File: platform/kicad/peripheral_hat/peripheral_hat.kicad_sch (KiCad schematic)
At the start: 48 parts, among them J1 Pi Header, J2 Pogo Pin, J3 Pogo Pin, J4 CRJ032-1-TH, J5 JST EH, J6 JST EH, T1 PT61018PEL, U1 LAN9500A-ABZJ

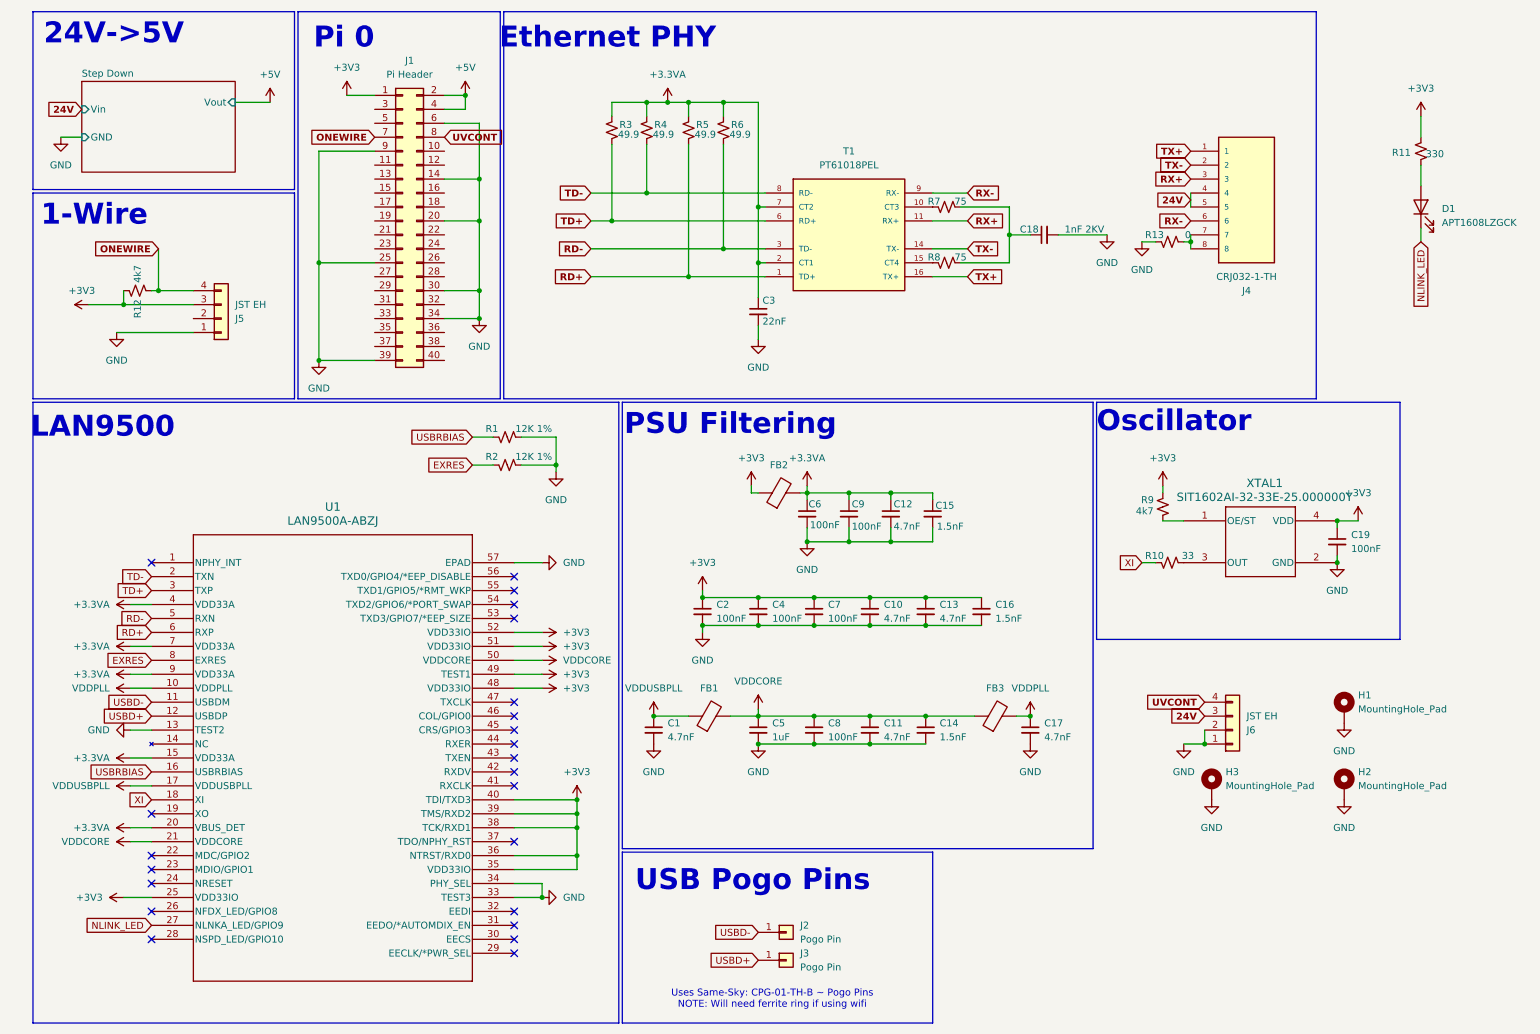
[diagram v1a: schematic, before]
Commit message: Peripheral Hat: Add MEMS I2C connector
This change adds a 5pin JST EH connector for connecting a I2S MEMS
device.
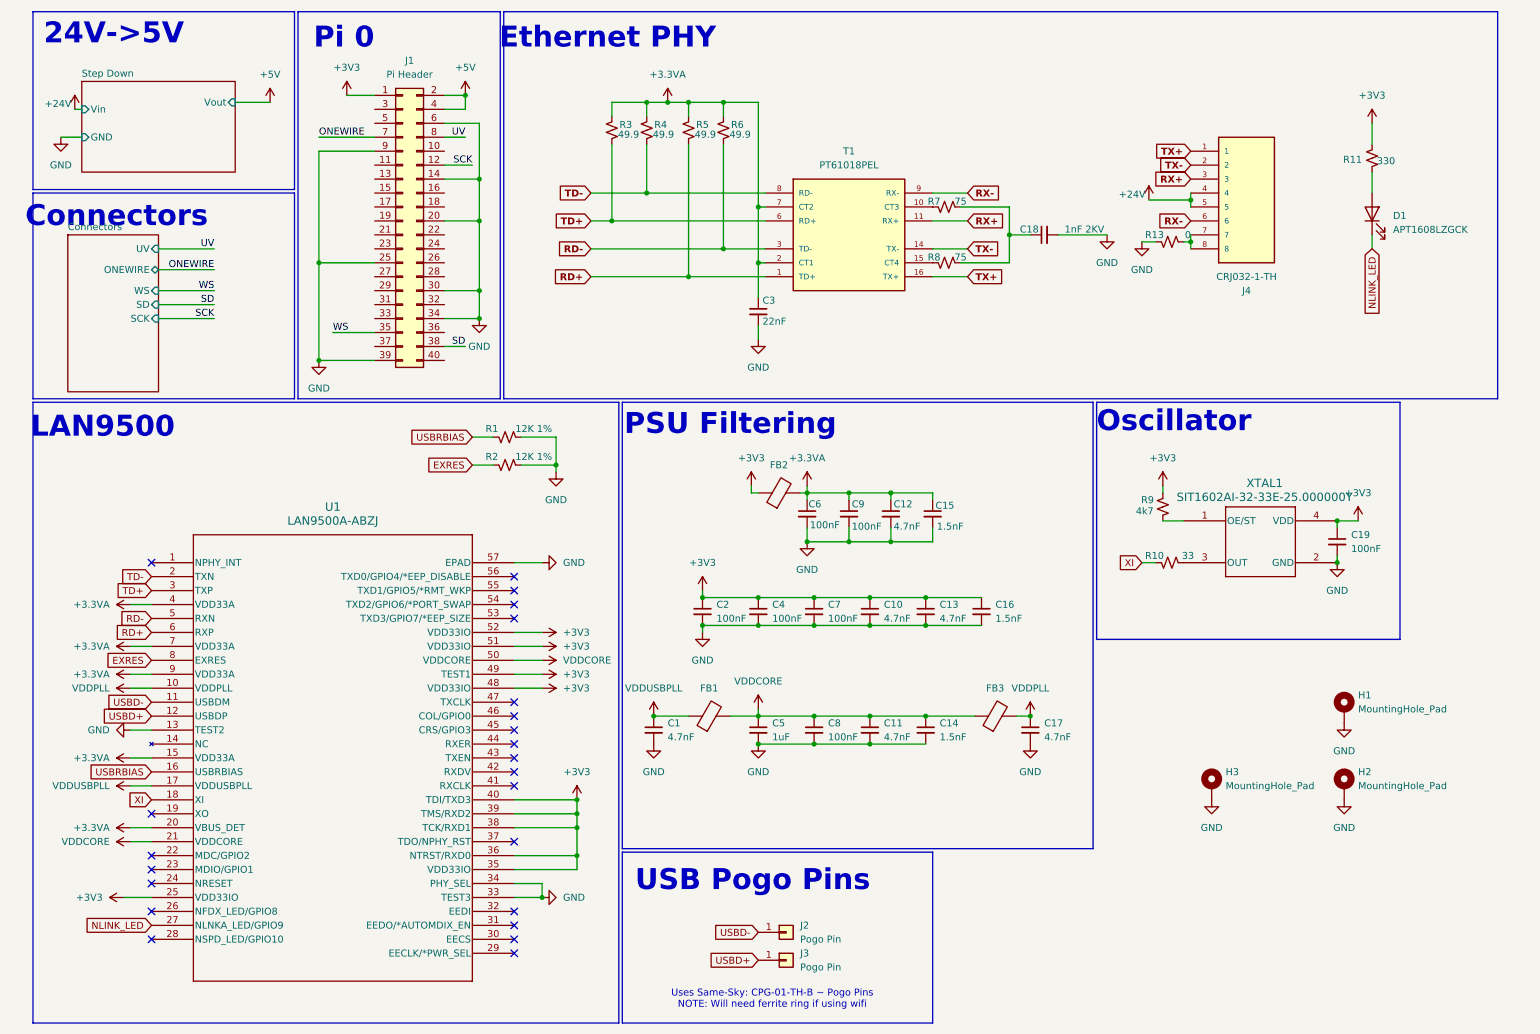
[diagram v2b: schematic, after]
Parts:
- removed J5, J6: JST EH, Connector_JST:JST_EH_B4B-EH-A_1x04_P2.50mm_Vertical, symbol Connector_Generic:Conn_01x04
- removed R12: 4k7, Resistor_SMD:R_0402_1005Metric, symbol Device:R_Small_US
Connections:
- net SCK: now reaches J1.12 (Pin_12)
- net WS: now reaches J1.35 (Pin_35)
- net SD: now reaches J1.38 (Pin_38)
- net 24V renamed +24V
- net UVCONT renamed UV
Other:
- added sheet Connectors (connectors.kicad_sch)
- note added: "Connectors"
- note removed: "1-Wire"
- moved on the sheet: D1, R11

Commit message: WIP: Save before deleting progress
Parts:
- removed J2, J3: Pogo Pin, AusOcean:YZP0009-20130-01, symbol Connector_Generic:Conn_01x01
- added J8: USB_B, Connector_USB:USB_Micro-B_Molex_47346-0001, symbol Connector:USB_B
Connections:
- net GND: now also J8.4 (GND), J8.5 (Shield)
- net USBD+: now also J8.3 (D+)
- net USBD-: now also J8.2 (D-)
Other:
- note removed: "Uses Same-Sky: CPG-01-TH-B ~ Pogo Pins NOTE: Will need ferrite ring if using wifi"

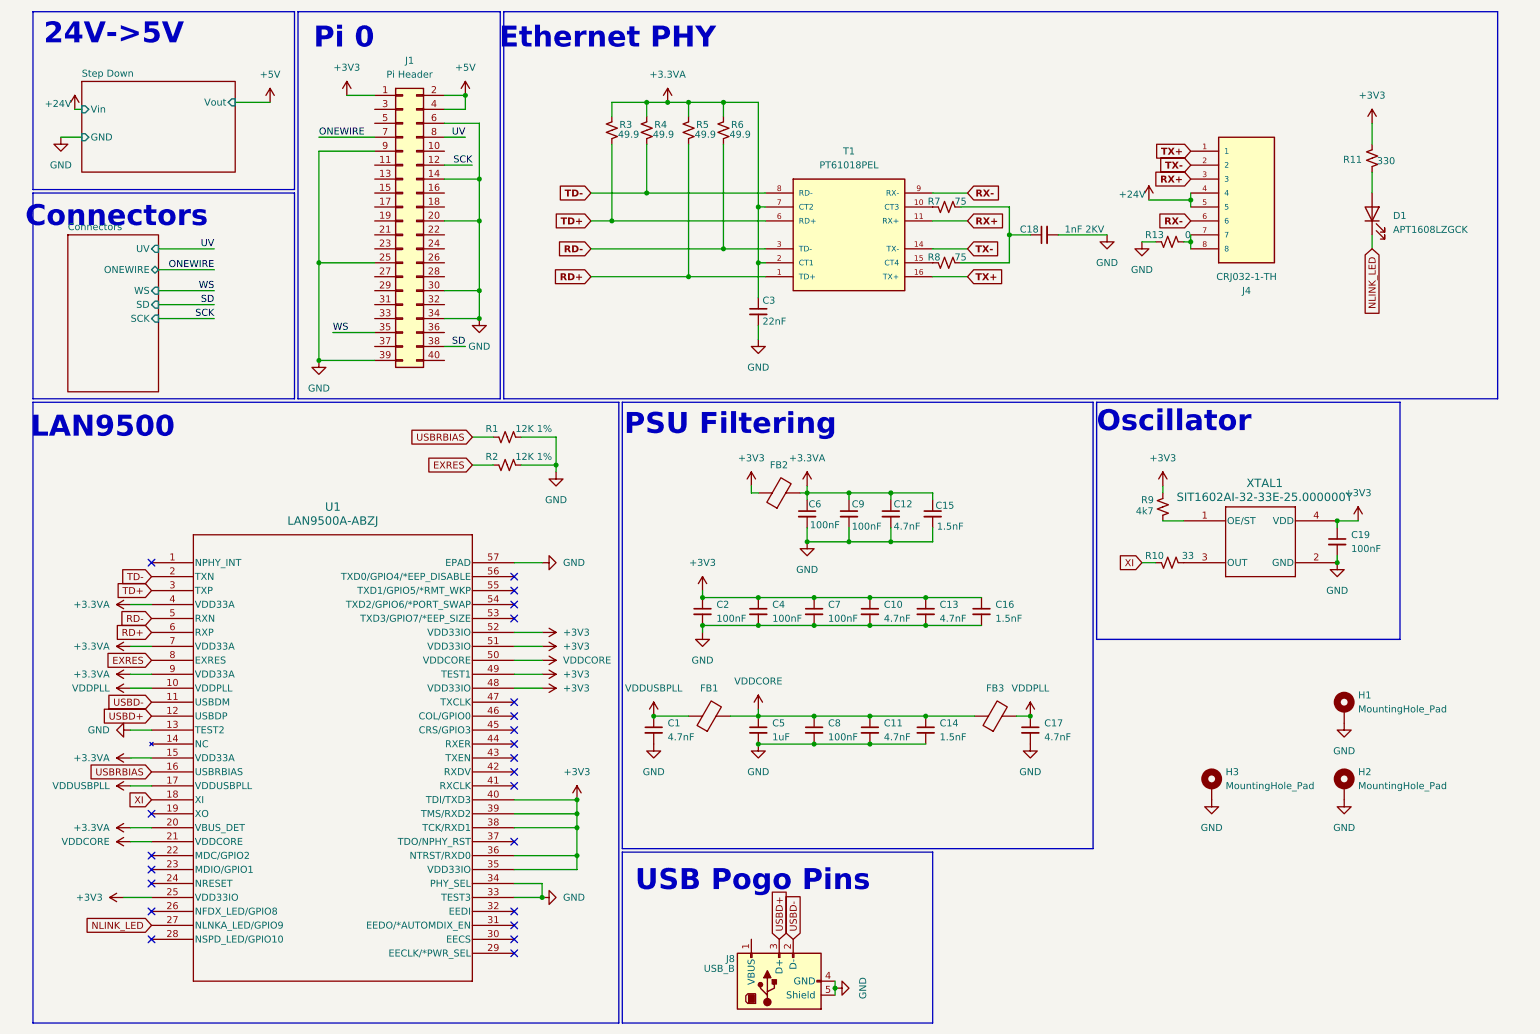
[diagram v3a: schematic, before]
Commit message: Peripheral Hat: V2 Rev C
Updates to using a micro-B interface between the pi and the hat.
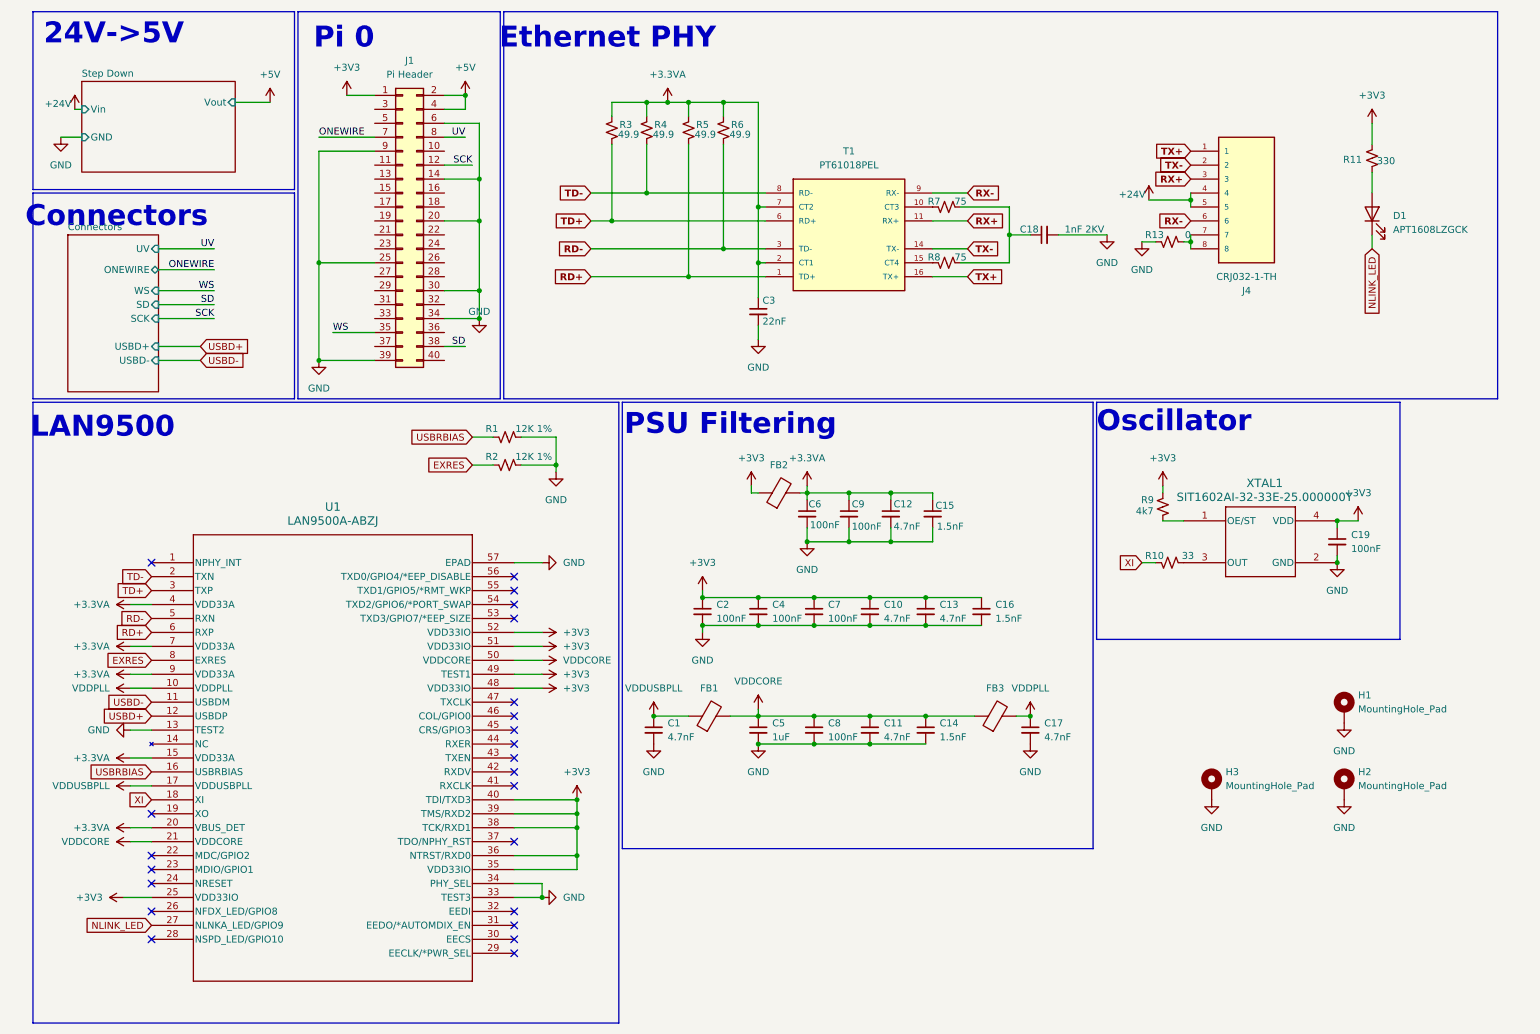
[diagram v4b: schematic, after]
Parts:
- removed J8: USB_B, Connector_USB:USB_Micro-B_Molex_47346-0001, symbol Connector:USB_B
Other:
- sheet Connectors ports: added USBD+, USBD-; removed none
- note removed: "USB Pogo Pins"
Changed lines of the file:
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@@
 		)
 	)
-	(rectangle
-		(start 120.015 165.735)
-		(end 176.53 196.85)
-		(stroke
-			(width 0)
-			(type default)
-		)
-		(fill
-			(type none)
-		)
-	)
 	(text "PSU Filtering"
 		(exclude_from_sim no)
@@
 		)
 	)
-	(text "USB Pogo Pins"
-		(exclude_from_sim no)
-		(at 143.764 170.942 0)
-		(effects
-			(font
-				(size 3.81 3.81)
-				(thickness 0.762)
-				(bold yes)
-			)
-		)
-	)
 	(text "Ethernet PHY"
 		(exclude_from_sim no)
@@
 	)
 	(junction
+		(at 111.76 166.37)
+		(diameter 0)
+		(color 0 0 0 0)
+	)
+	(junction
 		(at 154.94 124.46)
 		(diameter 0)
@@
 	)
 	(junction
-		(at 158.75 190.5)
-		(diameter 0)
-		(color 0 0 0 0)
-	)
-	(junction
 		(at 138.43 55.88)
 		(diameter 0)
@@
 		(color 0 0 0 0)
 	)
-	(junction
-		(at 111.76 166.37)
-		(diameter 0)
-		(color 0 0 0 0)
-	)
 	(no_connect
 		(at 100.33 176.53)
@@
 	(wire
 		(pts
+			(xy 43.18 73.66) (xy 35.56 73.66)
+		)
+		(stroke
+			(width 0)
+			(type default)
+		)
+	)
+	(wire
+		(pts
 			(xy 35.56 59.69) (xy 45.72 59.69)
 		)
@@
 	(wire
 		(pts
-			(xy 158.75 190.5) (xy 158.75 189.23)
-		)
-		(stroke
-			(width 0)
-			(type default)
-		)
-	)
-	(wire
-		(pts
 			(xy 250.19 105.41) (xy 250.19 106.68)
 		)
@@
 	(wire
 		(pts
+			(xy 111.76 166.37) (xy 111.76 168.91)
+		)
+		(stroke
+			(width 0)
+			(type default)
+		)
+	)
+	(wire
+		(pts
 			(xy 35.56 68.58) (xy 45.72 68.58)
 		)
@@
 	(wire
 		(pts
-			(xy 111.76 166.37) (xy 111.76 168.91)
-		)
-		(stroke
-			(width 0)
-			(type default)
-		)
-	)
-	(wire
-		(pts
 			(xy 190.5 53.34) (xy 194.31 53.34)
 		)
@@
 	(wire
 		(pts
-			(xy 158.75 191.77) (xy 158.75 190.5)
-		)
-		(stroke
-			(width 0)
-			(type default)
-		)
-	)
-	(wire
-		(pts
 			(xy 134.62 119.38) (xy 144.78 119.38)
 		)
@@
 	(wire
 		(pts
+			(xy 43.18 76.2) (xy 35.56 76.2)
+		)
+		(stroke
+			(width 0)
+			(type default)
+		)
+	)
+	(wire
+		(pts
 			(xy 176.53 109.22) (xy 176.53 106.68)
 		)
@@
 		)
 	)
-	(global_label "RX+"
+	(global_label "USBD+"
 		(shape input)
-		(at 223.52 43.18 180)
+		(at 43.18 73.66 0)
 		(fields_autoplaced yes)
 		(effects
 			(font
 				(size 1.27 1.27)
-				(bold yes)
 			)
-			(justify right)
+			(justify left)
 		)
 		(property "Intersheetrefs" "${INTERSHEET_REFS}"
-			(at 216.0069 43.18 0)
+			(at 51.8984 73.66 0)
 			(hide yes)
 			(show_name no)
@@
 					(size 1.27 1.27)
 				)
-				(justify right)
+				(justify left)
 			)
 		)
 	)
-	(global_label "USBD+"
+	(global_label "RX+"
 		(shape input)
-		(at 148.59 181.61 90)
+		(at 223.52 43.18 180)
 		(fields_autoplaced yes)
 		(effects
 			(font
 				(size 1.27 1.27)
+				(bold yes)
 			)
-			(justify left)
+			(justify right)
 		)
 		(property "Intersheetrefs" "${INTERSHEET_REFS}"
-			(at 148.59 172.8916 90)
+			(at 216.0069 43.18 0)
 			(hide yes)
 			(show_name no)
@@
 					(size 1.27 1.27)
 				)
-				(justify left)
+				(justify right)
 			)
 		)
@@
 		)
 	)
+	(global_label "USBD-"
+		(shape input)
+		(at 43.18 76.2 0)
+		(fields_autoplaced yes)
+		(effects
+			(font
+				(size 1.27 1.27)
+			)
+			(justify left)
+		)
+		(property "Intersheetrefs" "${INTERSHEET_REFS}"
+			(at 51.4889 76.2 0)
+			(hide yes)
+			(show_name no)
+			(do_not_autoplace no)
+			(effects
+				(font
+					(size 1.27 1.27)
+				)
+				(justify left)
+			)
+		)
+	)
 	(global_label "RD-"
 		(shape input)
@@
 		)
 	)
-	(global_label "USBD-"
-		(shape input)
-		(at 151.13 181.61 90)
-		(fields_autoplaced yes)
-		(effects
-			(font
-				(size 1.27 1.27)
-			)
-			(justify left)
-		)
-		(property "Intersheetrefs" "${INTERSHEET_REFS}"
-			(at 151.13 173.3011 90)
-			(hide yes)
-			(show_name no)
-			(do_not_autoplace no)
-			(effects
-				(font
-					(size 1.27 1.27)
-				)
-				(justify left)
-			)
-		)
-	)
 	(global_label "EXRES"
 		(shape input)
@@
 	)
 	(symbol
-		(lib_id "power:GND")
-		(at 158.75 190.5 90)
-		(unit 1)
-		(body_style 1)
-		(exclude_from_sim no)
-		(in_bom yes)
-		(on_board yes)
-		(in_pos_files yes)
-		(dnp no)
-		(fields_autoplaced yes)
-		(property "Reference" "#PWR056"
-			(at 165.1 190.5 0)
-			(hide yes)
-			(show_name no)
-			(do_not_autoplace no)
-			(effects
-				(font
-					(size 1.27 1.27)
-				)
-			)
-		)
-		(property "Value" "GND"
-			(at 163.83 190.5 0)
-			(show_name no)
-			(do_not_autoplace no)
-			(effects
-				(font
-					(size 1.27 1.27)
-				)
-			)
-		)
-		(property "Footprint" ""
-			(at 158.75 190.5 0)
-			(hide yes)
-			(show_name no)
-			(do_not_autoplace no)
-			(effects
-				(font
-					(size 1.27 1.27)
-				)
-			)
-		)
-		(property "Datasheet" ""
-			(at 158.75 190.5 0)
-			(hide yes)
-			(show_name no)
-			(do_not_autoplace no)
-			(effects
-				(font
-					(size 1.27 1.27)
-				)
-			)
-		)
-		(property "Description" "Power symbol creates a global label with name \"GND\" , ground"
-			(at 158.75 190.5 0)
-			(hide yes)
-			(show_name no)
-			(do_not_autoplace no)
-			(effects
-				(font
-					(size 1.27 1.27)
-				)
-			)
-		)
-		(pin "1"
-		)
-		(instances
-			(project "peripheral_hat"
-				(path "/8dfa5814-59de-42fa-a019-7b76c06633d1"
-					(reference "#PWR056")
-					(unit 1)
-				)
-			)
-		)
-	)
-	(symbol
-		(lib_id "Connector:USB_B")
-		(at 148.59 189.23 90)
-		(unit 1)
-		(body_style 1)
-		(exclude_from_sim no)
-		(in_bom yes)
-		(on_board yes)
-		(in_pos_files yes)
-		(dnp no)
-		(property "Reference" "J8"
-			(at 139.7 185.166 90)
-			(show_name no)
-			(do_not_autoplace no)
-			(effects
-				(font
-					(size 1.27 1.27)
-				)
-			)
-		)
-		(property "Value" "USB_B"
-			(at 137.668 186.944 90)
-			(show_name no)
-			(do_not_autoplace no)
-			(effects
-				(font
-					(size 1.27 1.27)
-				)
-			)
-		)
-		(property "Footprint" "Connector_USB:USB_Micro-B_Molex_47346-0001"
-			(at 149.86 185.42 0)
-			(hide yes)
-			(show_name no)
-			(do_not_autoplace no)
-			(effects
-				(font
-					(size 1.27 1.27)
-				)
-			)
-		)
-		(property "Datasheet" ""
-			(at 149.86 185.42 0)
-			(hide yes)
-			(show_name no)
-			(do_not_autoplace no)
-			(effects
-				(font
-					(size 1.27 1.27)
-				)
-			)
-		)
-		(property "Description" "USB Type B connector"
-			(at 148.59 189.23 0)
-			(hide yes)
-			(show_name no)
-			(do_not_autoplace no)
-			(effects
-				(font
-					(size 1.27 1.27)
-				)
-			)
-		)
-		(pin "3"
-		)
-		(pin "4"
-		)
-		(pin "1"
-		)
-		(pin "5"
-		)
-		(pin "2"
-		)
-		(instances
-			(project "peripheral_hat"
-				(path "/8dfa5814-59de-42fa-a019-7b76c06633d1"
-					(reference "J8")
-					(unit 1)
-				)
-			)
-		)
-	)
-	(symbol
 		(lib_id "power:+3V3")
 		(at 29.21 173.99 90)
@@
 		(in_pos_files yes)
 		(dnp no)
-		(fields_autoplaced yes)
 		(property "Reference" "#PWR016"
 			(at 93.98 74.93 0)
@@
 		)
 		(property "Value" "GND"
-			(at 93.98 73.66 0)
+			(at 93.98 67.31 0)
 			(show_name no)
 			(do_not_autoplace no)
@@
 			(effects
 				(font
+					(size 1.27 1.27)
+				)
+				(justify right)
+			)
+		)
+		(pin "USBD+" input
+			(at 35.56 73.66 0)
+			(effects
+				(font
+					(size 1.27 1.27)
+				)
+				(justify right)
+			)
+		)
+		(pin "USBD-" input
+			(at 35.56 76.2 0)
+			(effects
+				(font
